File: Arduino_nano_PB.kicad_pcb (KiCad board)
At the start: 2 copper layers, 100 x 40 mm, 44 parts, among them CON1 BARREL_JACK, P1 CONN_01X02, P7 CONN_01X04, Q1 BC547, Q2 BC547, Q3 BC547, Q4 2N3904BU, Q5 2N3904BU, Q6 2N3904BU, Q7 2N3904BU, Q8 2N3904BU, U1 LM7805CT, U2 74HC595, U3 Matriz_5x7, U4 Arduino_Nano

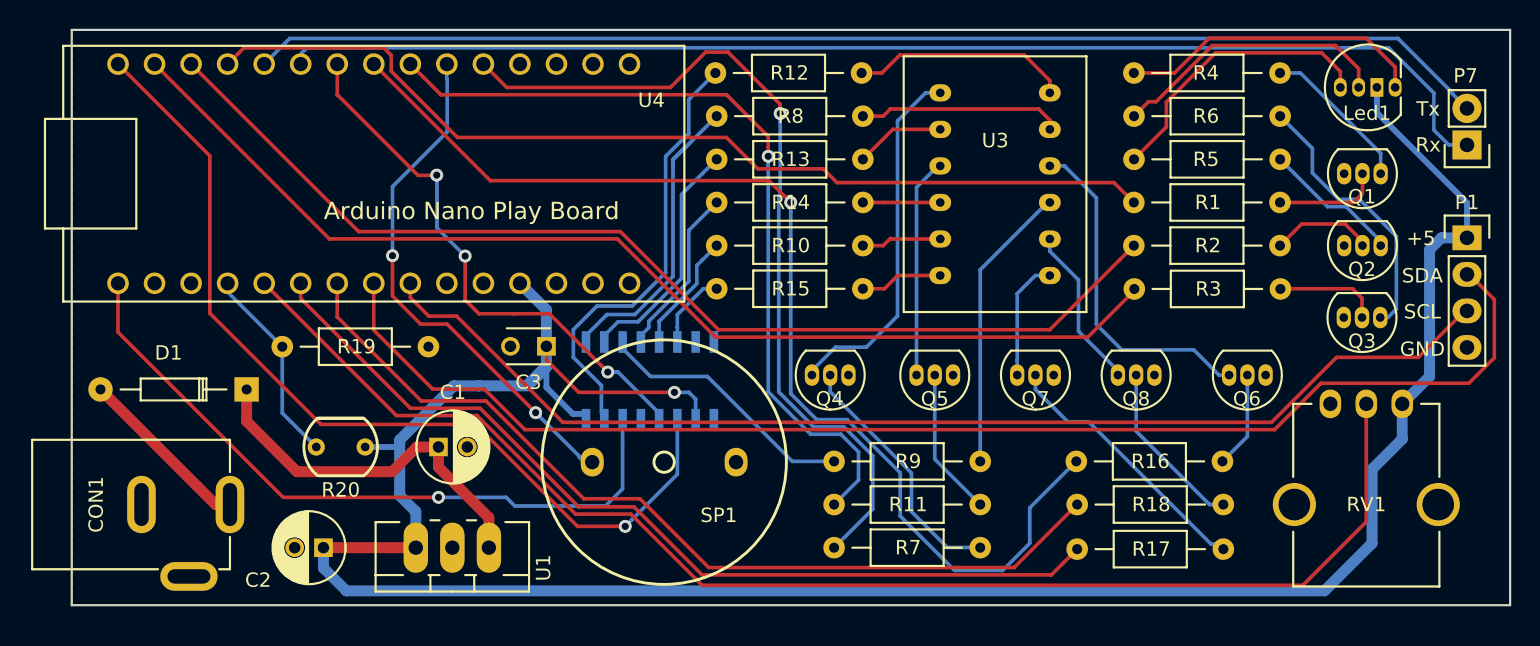
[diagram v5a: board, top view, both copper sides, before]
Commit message: añaadido zocalo para sensor de temperatura y primera distribucion sobre la PCB
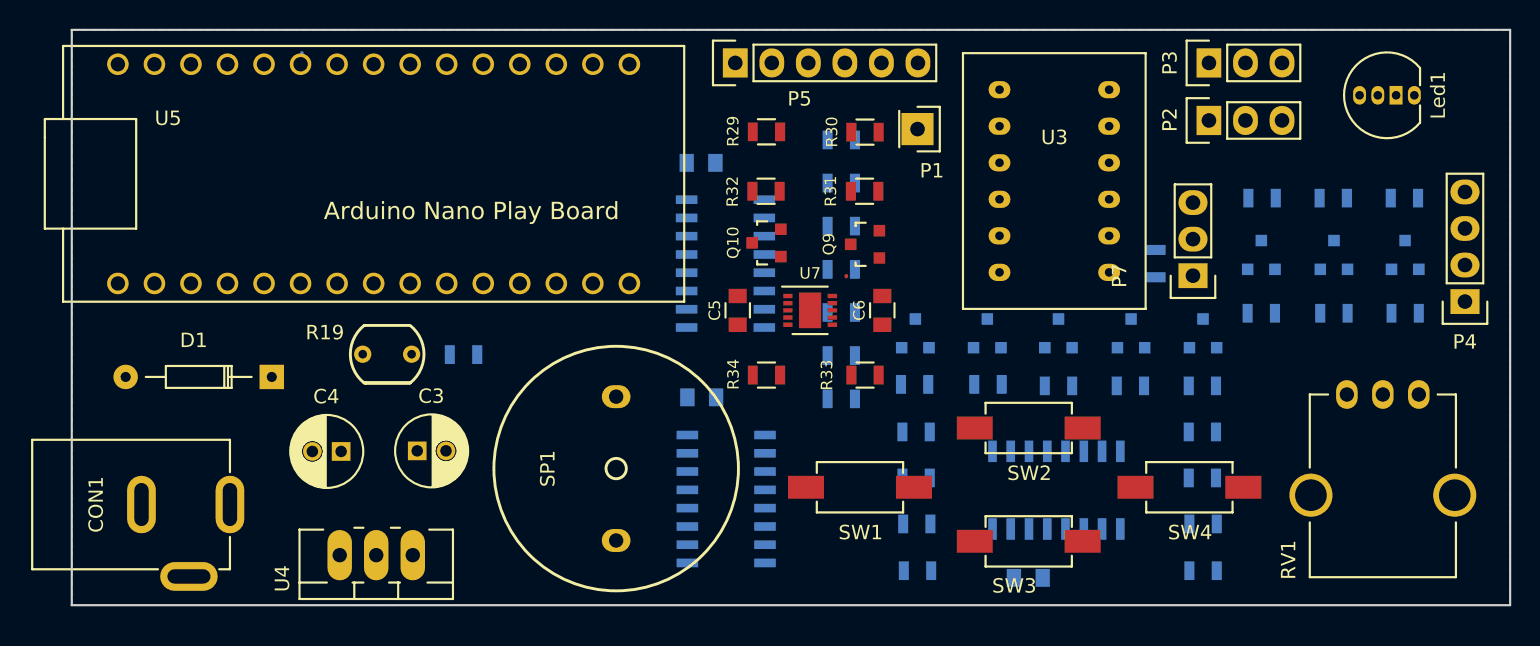
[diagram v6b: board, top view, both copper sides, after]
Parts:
- removed G***: LOGO, logos:logo_HackLabAl
- removed G***: LOGO, logos:osh-logo
- added C4: 0,1u, Capacitors_ThroughHole:C_Radial_D5_L11_P2, F.Cu at (128.7, 69.3)
- added C5: 100n, Capacitors_SMD:C_0805, F.Cu at (156.3, 59.5)
- added C6: 100n, Capacitors_SMD:C_0805, F.Cu at (166.3, 59.5)
- added C7: 100n, Capacitors_SMD:C_0805, B.Cu at (176.5, 78.1)
- added P2: CONN_01X03, Pin_Headers:Pin_Header_Straight_1x03, F.Cu at (189.1, 46.3)
- added P3: CONN_01X03, Pin_Headers:Pin_Header_Straight_1x03, F.Cu at (189.1, 42.3)
- added P4: CONN_01X04, Socket_Strips:Socket_Strip_Straight_1x04, F.Cu at (206.9, 58.9)
- added P5: CONN_01X06, Socket_Strips:Socket_Strip_Straight_1x06, F.Cu at (156.1, 42.3)
- added Q10: BSS138, TO_SOT_Packages_SMD:SOT-23, F.Cu at (158.3, 54.8)
- added Q9: BSS138, TO_SOT_Packages_SMD:SOT-23, F.Cu at (165.2, 54.9)
- added R21: 10K, Resistors_SMD:R_0805, B.Cu at (168.8, 77.6)
- added R22: 10K, Resistors_SMD:R_0805, B.Cu at (188.7, 77.6)
- added R23: 10K, Resistors_SMD:R_0805, B.Cu at (188.7, 74.3)
- added R24: 10K, Resistors_SMD:R_0805, B.Cu at (188.6, 68.0)
- added R25: 10K, Resistors_SMD:R_0805, B.Cu at (188.6, 71.2)
- added R26: 10K, Resistors_SMD:R_0805, B.Cu at (168.7, 68.0)
- added R27: 10K, Resistors_SMD:R_0805, B.Cu at (168.8, 74.3)
- added R28: 10K, Resistors_SMD:R_0805, B.Cu at (168.7, 71.2)
- added R29: 2K, Resistors_SMD:R_0805, F.Cu at (158.3, 47.1)
- added R30: 1K, Resistors_SMD:R_0805, F.Cu at (165.2, 47.1)
- added R31: 4K7, Resistors_SMD:R_0805, F.Cu at (165.1, 51.2)
- added R32: 4K7, Resistors_SMD:R_0805, F.Cu at (158.3, 51.2)
- added R33: 4K7, Resistors_SMD:R_0805, F.Cu at (165.2, 64.0)
- added R34: 4K7, Resistors_SMD:R_0805, F.Cu at (158.3, 64.0)
- added R35: R, Resistors_SMD:R_0805, B.Cu at (185.4, 56.2)
- added SW1: Izquierda, Relays_and_Contacts:CANAL_ELECTRONIC_DTSM-31N-B, F.Cu at (164.8, 71.8)
- added SW2: Arriba, Relays_and_Contacts:CANAL_ELECTRONIC_DTSM-31N-B, F.Cu at (176.5, 67.7)
- added SW3: Abajo, Relays_and_Contacts:CANAL_ELECTRONIC_DTSM-31N-B, F.Cu at (176.5, 75.6)
- added SW4: Derecha, Relays_and_Contacts:CANAL_ELECTRONIC_DTSM-31N-B, F.Cu at (187.7, 71.8)
- added U5: Arduino_Nano, Arduino:Arduino_Nano, F.Cu at (131.0, 50.0)
- added U6: 74HC148, Housings_SOIC:SOIC-16_3.9x9.9mm_Pitch1.27mm, B.Cu at (178.5, 72.0)
- added U7: MMA7660FC, Housings_DFN_QFN:DFN-10-1EP_3x3mm_Pitch0.5mm, F.Cu at (161.3, 59.5)
- C1: value 0,33u -> 100n; footprint Capacitors_ThroughHole:C_Radial_D5_L11_P2 -> Capacitors_SMD:C_0805; moved to B.Cu
- C2: value 0,1u -> 100n; footprint Capacitors_ThroughHole:C_Radial_D5_L11_P2 -> Capacitors_SMD:C_0805; moved to B.Cu
- C3: value 100n -> 0,33u; footprint Capacitors_ThroughHole:C_Disc_D3_P2.5 -> Capacitors_ThroughHole:C_Radial_D5_L11_P2
- P1: value CONN_01X02 -> CONN_01X01; footprint Pin_Headers:Pin_Header_Straight_1x02 -> Socket_Strips:Socket_Strip_Straight_1x01
- P7: value CONN_01X04 -> CONN_01X03; footprint Pin_Headers:Pin_Header_Straight_1x04 -> Socket_Strips:Socket_Strip_Straight_1x03
- Q1, Q2, Q3: value BC547 -> SMBT3904; footprint Transistors:TO-92_EnLinea_Estrecho_Oval -> TO_SOT_Packages_SMD:SOT-23; moved to B.Cu
- Q4, Q5: value 2N3904BU -> SMBT3904; footprint Transistors:TO-92_EnLinea_Estrecho_Oval -> TO_SOT_Packages_SMD:SOT-23; moved to B.Cu
- Q6, Q7, Q8: value 2N3904BU -> BC846B; footprint Transistors:TO-92_EnLinea_Estrecho_Oval -> TO_SOT_Packages_SMD:SOT-23; moved to B.Cu
- R1: value 4K7 -> 1K; footprint Resistencias:Resistencia_1_4_W_10_mm -> Resistors_SMD:R_0805; moved to B.Cu
- R10, R12: value 120 -> 1K; footprint Resistencias:Resistencia_1_4_W_10_mm -> Resistors_SMD:R_0805; moved to B.Cu
- R11, R8, R9: footprint Resistencias:Resistencia_1_4_W_10_mm -> Resistors_SMD:R_0805; moved to B.Cu
- R13, R14, R15: value 120 -> 4K7; footprint Resistencias:Resistencia_1_4_W_10_mm -> Resistors_SMD:R_0805; moved to B.Cu
- R16, R17, R18: value 1K -> 100; footprint Resistencias:Resistencia_1_4_W_10_mm -> Resistors_SMD:R_0805; moved to B.Cu
- R19: value 1K -> LDR; footprint Resistencias:Resistencia_1_4_W_10_mm -> Sensores:LDR_TOKEN_PGM5_Series
- R2, R3: value 4K7 -> 120; footprint Resistencias:Resistencia_1_4_W_10_mm -> Resistors_SMD:R_0805; moved to B.Cu
- R20: value LDR -> 1K; footprint Sensores:LDR_TOKEN_PGM5_Series -> Resistors_SMD:R_0805; moved to B.Cu
- R4, R6: value 100 -> 120; footprint Resistencias:Resistencia_1_4_W_10_mm -> Resistors_SMD:R_0805; moved to B.Cu
- R5: value 100 -> 1K; footprint Resistencias:Resistencia_1_4_W_10_mm -> Resistors_SMD:R_0805; moved to B.Cu
- R7: value 1K -> 120; footprint Resistencias:Resistencia_1_4_W_10_mm -> Resistors_SMD:R_0805; moved to B.Cu
- U1: value LM7805CT -> 74HC595; footprint TO_SOT_Packages_THT:TO-220_Neutral123_Vertical_LargePads -> Housings_SOIC:SOIC-16_3.9x9.9mm_Pitch1.27mm; moved to B.Cu
- U4: value Arduino_Nano -> LM7805CT; footprint Arduino:Arduino_Nano -> TO_SOT_Packages_THT:TO-220_Neutral123_Vertical_LargePads
- moved R13 39.2 mm to (202.7, 59.7)
- moved P1 38.2 mm to (168.8, 46.9)
- moved C2 37.5 mm to (153.8, 49.2), turned to 0 degrees
- moved Q1 34.2 mm to (168.7, 61.1)
- moved R14 33.6 mm to (197.8, 59.7)
- moved R12 32.2 mm to (188.6, 64.8)
- moved R2 30.8 mm to (163.5, 50.6)
- moved R3 30.6 mm to (163.5, 56.6)
- moved R1 28.4 mm to (168.6, 64.7)
- moved R4 28.3 mm to (163.5, 62.6), turned to 180 degrees
- moved Q2 28.0 mm to (173.7, 61.1)
- moved R15 27.8 mm to (192.7, 59.7)
- moved U1 27.4 mm to (155.4, 56.2)
- moved U4 26.5 mm to (131.2, 76.5)
- moved R17 25.6 mm to (197.7, 51.7)
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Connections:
- C1 pad 1: Net-(C1-Pad1) -> +5V
- C3 pad 1: +5V -> Net-(C3-Pad1)
- D1 pad 1: Net-(C1-Pad1) -> Net-(C3-Pad1)
- P1 pad 1: /D7 -> RESET
- P7 pad 2: /A4 -> A3
- P7 pad 3: /A5 -> Net-(P7-Pad3)
- Q1 pad 2: Net-(Q1-Pad2) -> GND
- Q1 pad 3: GND -> Net-(Q1-Pad3)
- Q2 pad 2: Net-(Q2-Pad2) -> GND
- Q2 pad 3: GND -> Net-(Q2-Pad3)
- Q3 pad 2: Net-(Q3-Pad2) -> GND
- Q3 pad 3: GND -> Net-(Q3-Pad3)
- Q4 pad 1: GND -> Net-(Q4-Pad1)
- Q4 pad 2: Net-(Q4-Pad2) -> GND
- Q5 pad 1: GND -> Net-(Q5-Pad1)
- Q5 pad 2: Net-(Q5-Pad2) -> GND
- Q6 pad 1: GND -> Net-(Q6-Pad1)
- Q6 pad 2: Net-(Q6-Pad2) -> GND
- Q7 pad 1: GND -> Net-(Q7-Pad1)
- Q7 pad 2: Net-(Q7-Pad2) -> GND
- Q8 pad 1: GND -> Net-(Q8-Pad1)
- Q8 pad 2: Net-(Q8-Pad2) -> GND
- R1 pad 1: Net-(Q1-Pad2) -> Net-(Q1-Pad1)
- R1 pad 2: /D9 -> Net-(R1-Pad2)
- R10 pad 1: Net-(R10-Pad1) -> Net-(Q3-Pad1)
- R11 pad 1: Net-(Q5-Pad2) -> Net-(Q4-Pad1)
- R11 pad 2: /D4 -> Net-(R11-Pad2)
- R12 pad 1: Net-(R12-Pad1) -> Net-(Q5-Pad1)
- R13 pad 1: Net-(R13-Pad1) -> Net-(Q6-Pad1)
- R13 pad 2: Net-(R13-Pad2) -> D9
- R14 pad 1: Net-(R14-Pad1) -> Net-(Q7-Pad1)
- R14 pad 2: Net-(R14-Pad2) -> D10
- R15 pad 1: Net-(R15-Pad1) -> Net-(Q8-Pad1)
- R15 pad 2: Net-(R15-Pad2) -> D11
- R16 pad 1: Net-(Q6-Pad2) -> Net-(Led1-Pad4)
- R16 pad 2: /D5 -> Net-(Q6-Pad3)
- R17 pad 1: Net-(Q7-Pad2) -> Net-(Led1-Pad1)
- R17 pad 2: /A2 -> Net-(Q7-Pad3)
- R18 pad 1: Net-(Q8-Pad2) -> Net-(Led1-Pad2)
- R18 pad 2: /A3 -> Net-(Q8-Pad3)
- R19 pad 1: GND -> +5V
- R19 pad 2: /A0 -> A6
- R2 pad 1: Net-(Q2-Pad2) -> Net-(R2-Pad1)
- R2 pad 2: /D10 -> Net-(R2-Pad2)
- R20 pad 1: +5V -> GND
- R20 pad 2: /A0 -> A6
- R3 pad 1: Net-(Q3-Pad2) -> Net-(R3-Pad1)
- R3 pad 2: /D11 -> Net-(R3-Pad2)
- R4 pad 1: Net-(Led1-Pad4) -> Net-(R4-Pad1)
- R4 pad 2: Net-(Q1-Pad1) -> Net-(R4-Pad2)
- R5 pad 1: Net-(Led1-Pad1) -> Net-(Q2-Pad1)
- R5 pad 2: Net-(Q2-Pad1) -> Net-(R5-Pad2)
- R6 pad 1: Net-(Led1-Pad2) -> Net-(R6-Pad1)
- R6 pad 2: Net-(Q3-Pad1) -> Net-(R6-Pad2)
- R7 pad 1: Net-(Q4-Pad2) -> Net-(R7-Pad1)
- R7 pad 2: /D2 -> Net-(R7-Pad2)
- RV1 pad 2: /A1 -> A7
- SP1 pad 1: /D3 -> D3
- U1 pad 1: Net-(C1-Pad1) -> Net-(R2-Pad2)
- U1 pad 2: GND -> Net-(R7-Pad2)
- U1 pad 3: +5V -> Net-(R3-Pad2)
- U2 pad 1: Net-(R8-Pad2) -> Net-(R5-Pad2)
- U2 pad 11: /D12 -> D13
- U2 pad 12: /D6 -> D4
- U2 pad 14: /D13 -> Net-(U1-Pad9)
- U2 pad 15: Net-(R12-Pad2) -> Net-(R1-Pad2)
- U2 pad 2: Net-(R13-Pad2) -> Net-(R10-Pad2)
- U2 pad 3: Net-(R9-Pad2) -> Net-(R11-Pad2)
- U2 pad 4: Net-(R14-Pad2) -> Net-(R12-Pad2)
- U2 pad 5: Net-(R10-Pad2) -> Net-(U2-Pad5)
- U2 pad 6: Net-(R15-Pad2) -> Net-(U2-Pad6)
- U3 pad 1: Net-(Q4-Pad3) -> Net-(Q1-Pad3)
- U3 pad 10: Net-(Q6-Pad3) -> Net-(Q3-Pad3)
- U3 pad 11: Net-(R8-Pad1) -> Net-(R2-Pad1)
- U3 pad 12: Net-(R12-Pad1) -> Net-(R6-Pad1)
- U3 pad 2: Net-(R13-Pad1) -> Net-(R7-Pad1)
- U3 pad 3: Net-(Q5-Pad3) -> Net-(Q2-Pad3)
- U3 pad 4: Net-(R14-Pad1) -> Net-(R8-Pad1)
- U3 pad 5: Net-(R10-Pad1) -> Net-(R4-Pad1)
- U3 pad 6: Net-(R15-Pad1) -> Net-(R9-Pad1)
- U3 pad 7: Net-(Q7-Pad3) -> Net-(Q4-Pad3)
- U3 pad 8: Net-(Q8-Pad3) -> Net-(Q5-Pad3)
- U3 pad 9: Net-(R9-Pad1) -> Net-(R3-Pad1)
- U4 pad 1: Net-(U4-Pad1) -> Net-(C3-Pad1)
- U4 pad 2: Net-(U4-Pad2) -> GND
- U4 pad 3: Net-(U4-Pad3) -> +5V
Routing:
- net +5V: track 176.5 -> 0.00 mm, vias 1 -> 0
- net /A1: track 95.3 -> 0.00 mm
- net /A4: track 92.8 -> 0.00 mm
- net /D8: track 86.4 -> 0.00 mm
- net /D7: track 86.3 -> 0.00 mm
- net /A5: track 81.3 -> 0.00 mm
- net /D5: track 77.5 -> 0.00 mm, vias 1 -> 0
- net /D11: track 77.5 -> 0.00 mm
- net /D10: track 75.6 -> 0.00 mm
- net /D9: track 68.6 -> 0.00 mm
- net /D12: track 63.9 -> 0.00 mm, vias 1 -> 0
- net /A2: track 63.7 -> 0.00 mm
- net /A3: track 62.8 -> 0.00 mm
- net /D2: track 59.7 -> 0.00 mm, vias 1 -> 0
- net /D4: track 57.1 -> 0.00 mm, vias 1 -> 0
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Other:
- board text removed: "+5"
- board text removed: "ClkIn-D12"
- board text removed: "ClkOut-D6"
- board text removed: "Col1-D2"
- board text removed: "Col2-D4"
- board text removed: "Col3-D5"
- board text removed: "Col4-A2"
- board text removed: "Col5-A3"
- board text removed: "Din-D13"
- board text removed: "GND"
- board text removed: "I2C"
- board text removed: "LDR-A0"
- board text removed: "Rx"
- board text removed: "Rx-D7"
- board text removed: "SCL"
- board text removed: "SDA"
- board text removed: "SERIAL"
- board text removed: "Tx"
- board text removed: "Tx-D8"

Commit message: finalizado enrutado provisional
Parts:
- added B1: Encoder_Inc, Sensores:Bourns_3315C_encoder_incremental, F.Cu at (118.1, 75.5)
- added C8: C, Capacitors_SMD:C_0805, B.Cu at (113.2, 69.4)
- added C9: C, Capacitors_SMD:C_0805, B.Cu at (123.0, 69.4)
- added Gnd-Via: VAL**, Vias:Gnd-Via, F.Cu at (156.4, 57.0)
- added Gnd-Via: VAL**, Vias:Gnd-Via, F.Cu at (186.0, 76.2)
- added Gnd-Via: VAL**, Vias:Gnd-Via, F.Cu at (131.4, 69.3)
- added Gnd-Via: VAL**, Vias:Gnd-Via, F.Cu at (154.5, 62.4)
- added Gnd-Via: VAL**, Vias:Gnd-Via, F.Cu at (154.8, 72.0)
- added Gnd-Via: VAL**, Vias:Gnd-Via, F.Cu at (147.1, 61.0)
- added Gnd-Via: VAL**, Vias:Gnd-Via, F.Cu at (151.5, 62.1)
- added Gnd-Via: VAL**, Vias:Gnd-Via, F.Cu at (161.7, 75.0)
- added Gnd-Via: VAL**, Vias:Gnd-Via, F.Cu at (176.7, 76.4)
- added Gnd-Via: VAL**, Vias:Gnd-Via, F.Cu at (154.4, 55.6)
- added R36: R, Resistors_SMD:R_0805, B.Cu at (113.2, 77.0)
- added R37: R, Resistors_SMD:R_0805, B.Cu at (113.2, 73.3)
- added R38: R, Resistors_SMD:R_0805, B.Cu at (123.0, 77.0)
- added R39: R, Resistors_SMD:R_0805, B.Cu at (123.0, 73.3)
- D1: footprint Diodes_ThroughHole:Diode_DO-35_SOD27_Horizontal_RM10 -> Diodos:DO-214AC
- moved R33 12.3 mm to (165.2, 51.8), turned to 0 degrees
- moved R34 12.3 mm to (158.3, 51.8), turned to 0 degrees
- moved R31 11.7 mm to (165.1, 62.9)
- moved R32 11.7 mm to (158.2, 62.9)
- moved CON1 7.59 mm to (120.8, 65.4)
- moved Q7 5.15 mm to (192.6, 55.6)
- moved R14 5.15 mm to (192.6, 59.6)
- moved R17 5.15 mm to (192.6, 51.6)
- moved Q8 5.05 mm to (197.8, 55.6)
- moved R15 5.05 mm to (197.8, 59.7)
- moved R18 5.05 mm to (197.8, 51.7)
- moved R20 0.26 mm to (137.0, 62.6)
- moved Led1 0.25 mm to (201.7, 44.5)
- moved D1 0.24 mm to (124.0, 63.9), turned to 90 degrees
- moved R21 0.09 mm to (168.7, 77.6)
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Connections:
- P4 pad 2: D7 -> D8
- P4 pad 3: D8 -> D7
- P5 pad 1: A2 -> Net-(P5-Pad1)
- P7 pad 3: Net-(P7-Pad3) -> GND
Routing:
- net +5V: track 0.00 -> 486.2 mm, vias 0 -> 7
- net D8: track 0.00 -> 101.6 mm
- net D7: track 0.81 -> 100.9 mm
- net D11: track 0.00 -> 99.7 mm, vias 0 -> 1
- net D9: track 0.00 -> 98.8 mm, vias 0 -> 1
- net +3V3: track 0.00 -> 91.8 mm, vias 0 -> 2
- net D10: track 0.00 -> 91.8 mm, vias 0 -> 1
- net A1: track 0.00 -> 91.6 mm, vias 0 -> 1
- net A3: track 0.00 -> 81.5 mm, vias 0 -> 2
- net A7: track 0.00 -> 78.9 mm, vias 0 -> 1
- net A0: track 0.00 -> 77.0 mm, vias 0 -> 1
- net D6: track 0.00 -> 70.0 mm, vias 0 -> 2
- net D5: track 0.00 -> 65.6 mm, vias 0 -> 2
- net D13: track 0.00 -> 65.5 mm
- net A4: track 0.00 -> 61.5 mm, vias 0 -> 2
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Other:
- net class Default: clearance 0.254 -> 0.2032
- net class Power: trace_width 0.4064 -> 0.6096; via_dia 0.7 -> 1
- rule trace_clearance: 0.254 -> 0.2032
